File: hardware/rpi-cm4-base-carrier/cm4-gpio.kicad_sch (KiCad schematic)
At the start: 15 parts, among them J1 DNP, J2 USB4105-GF-A, J3 SM04B-SRSS-TB(LF)(SN), U1 74LVC1G07SE-7

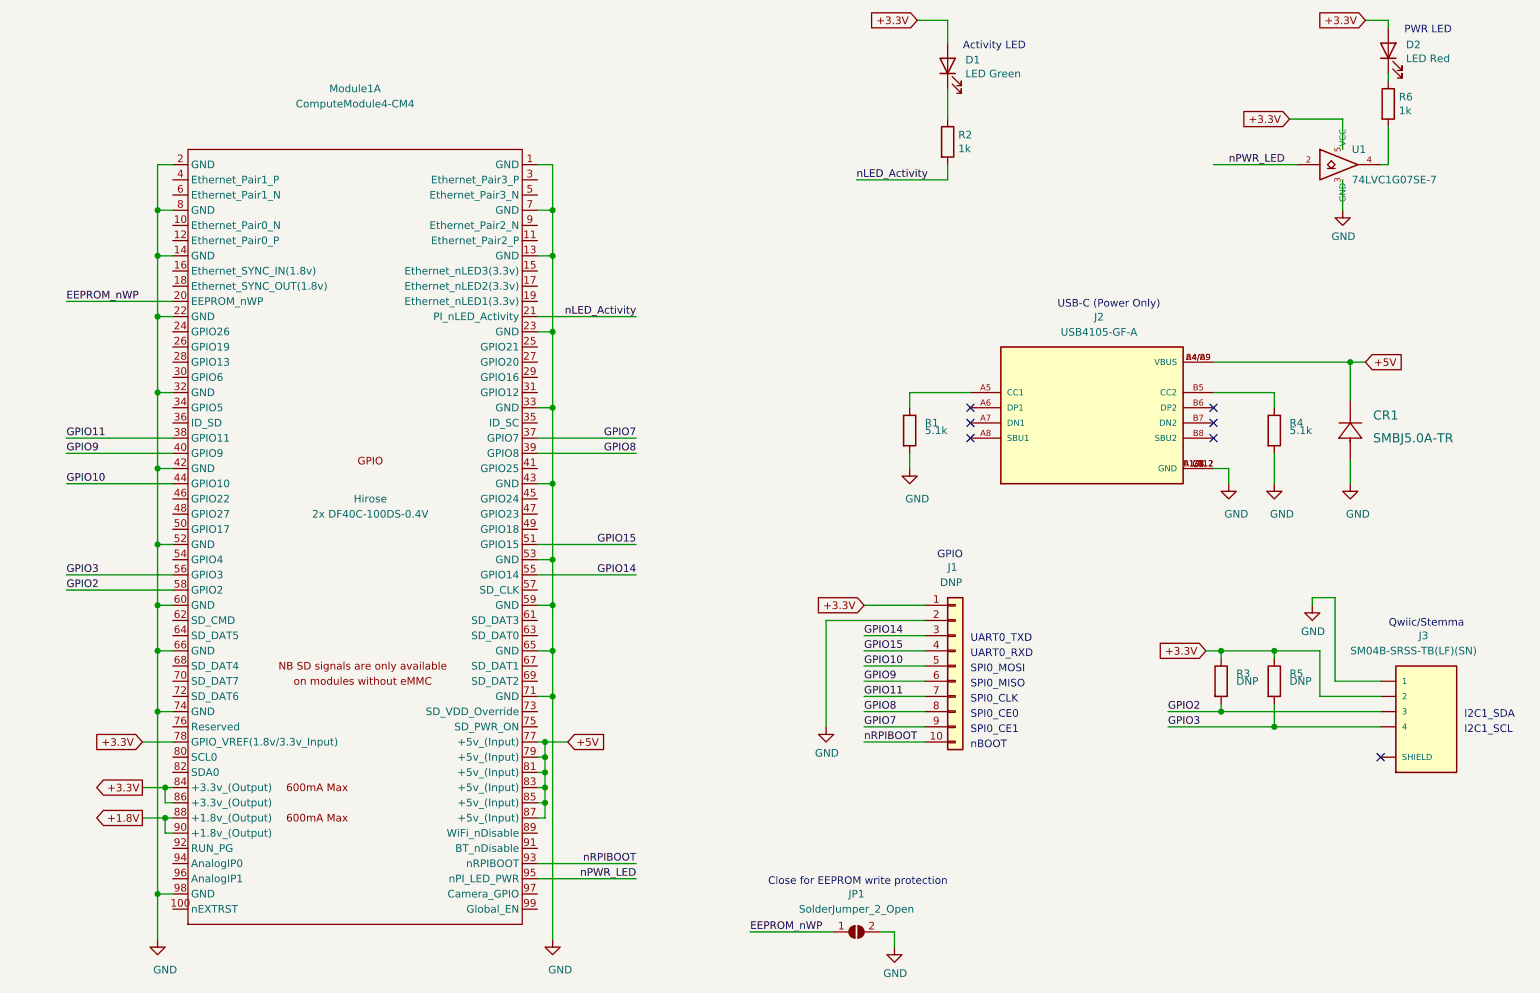
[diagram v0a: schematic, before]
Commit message: schematic changes to add network, hdmi, usbhost and SD
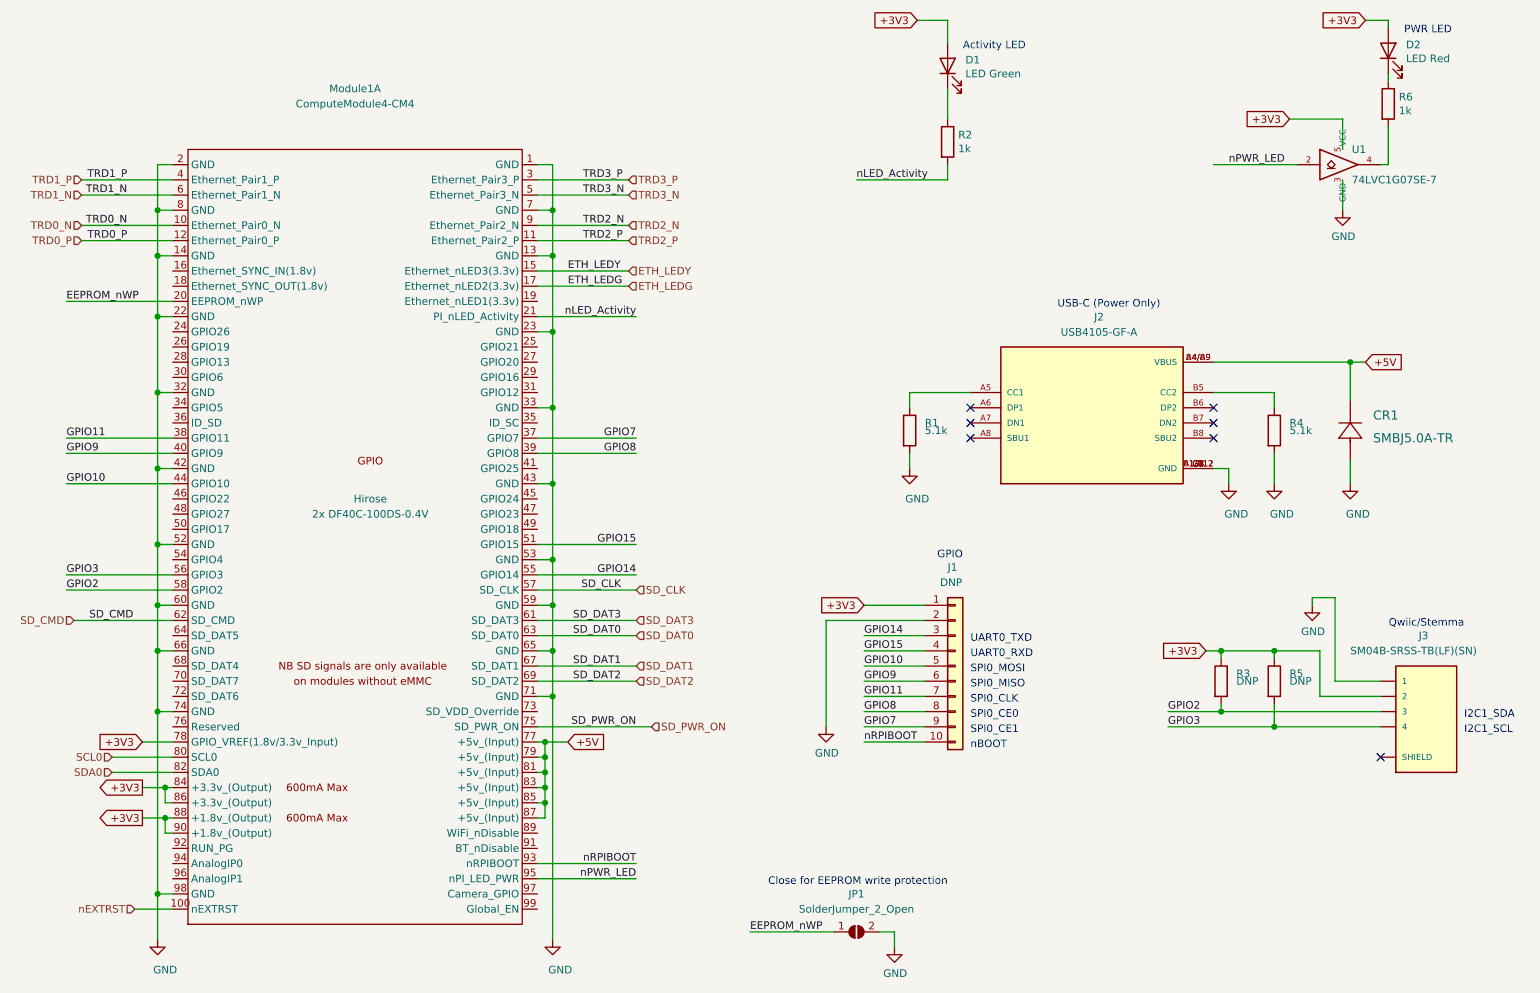
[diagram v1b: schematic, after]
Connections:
- net +3.3V is gone; now on net +3V3: D1.2 (A), D2.2 (A), J1.1 (Pin_1), J3.2, Module1.78 (GPIO_VREF(1.8v/3.3v_Input)), Module1.84 (+3.3v_(Output)), Module1.86 (+3.3v_(Output)), R3.1, R5.1, U1.5 (VCC)
- net TRD0_N: now reaches Module1.10 (Ethernet_Pair0_N)
- net nEXTRST: now reaches Module1.100 (nEXTRST)
- net TRD2_P: now reaches Module1.11 (Ethernet_Pair2_P)
- net TRD0_P: now reaches Module1.12 (Ethernet_Pair0_P)
- net ETH_LEDY: now reaches Module1.15 (Ethernet_nLED3(3.3v))
- net ETH_LEDG: now reaches Module1.17 (Ethernet_nLED2(3.3v))
- net TRD3_P: now reaches Module1.3 (Ethernet_Pair3_P)
- net TRD1_P: now reaches Module1.4 (Ethernet_Pair1_P)
- net TRD3_N: now reaches Module1.5 (Ethernet_Pair3_N)
- net SD_CLK: now reaches Module1.57 (SD_CLK)
- net TRD1_N: now reaches Module1.6 (Ethernet_Pair1_N)
- net SD_DAT3: now reaches Module1.61 (SD_DAT3)
- net SD_CMD: now reaches Module1.62 (SD_CMD)
- net SD_DAT0: now reaches Module1.63 (SD_DAT0)
- net SD_DAT1: now reaches Module1.67 (SD_DAT1)
- net SD_DAT2: now reaches Module1.69 (SD_DAT2)
- net SD_PWR_ON: now reaches Module1.75 (SD_PWR_ON)
- net SCL0: now reaches Module1.80 (SCL0)
- net SDA0: now reaches Module1.82 (SDA0)
- net TRD2_N: now reaches Module1.9 (Ethernet_Pair2_N)
- net +1.8V renamed +3V3
